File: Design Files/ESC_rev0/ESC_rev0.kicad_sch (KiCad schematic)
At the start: 0 parts

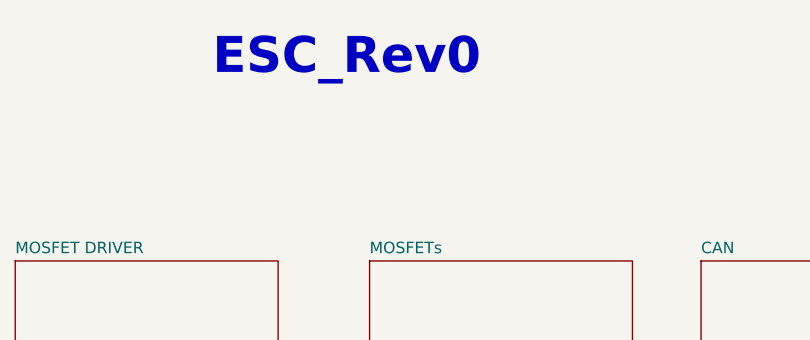
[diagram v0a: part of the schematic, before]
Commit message: update 6
gate driver completion and mosfet init
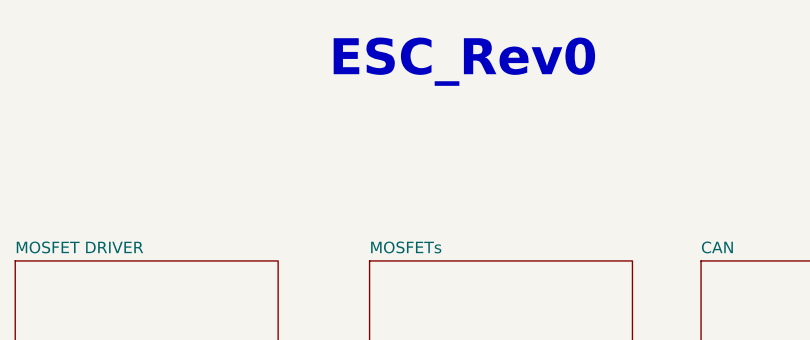
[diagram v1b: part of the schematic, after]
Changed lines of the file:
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@@
 	(text "${TITLE}"
 		(exclude_from_sim no)
-		(at 130.81 21.844 0)
+		(at 143.764 22.098 0)
 		(effects
 			(font

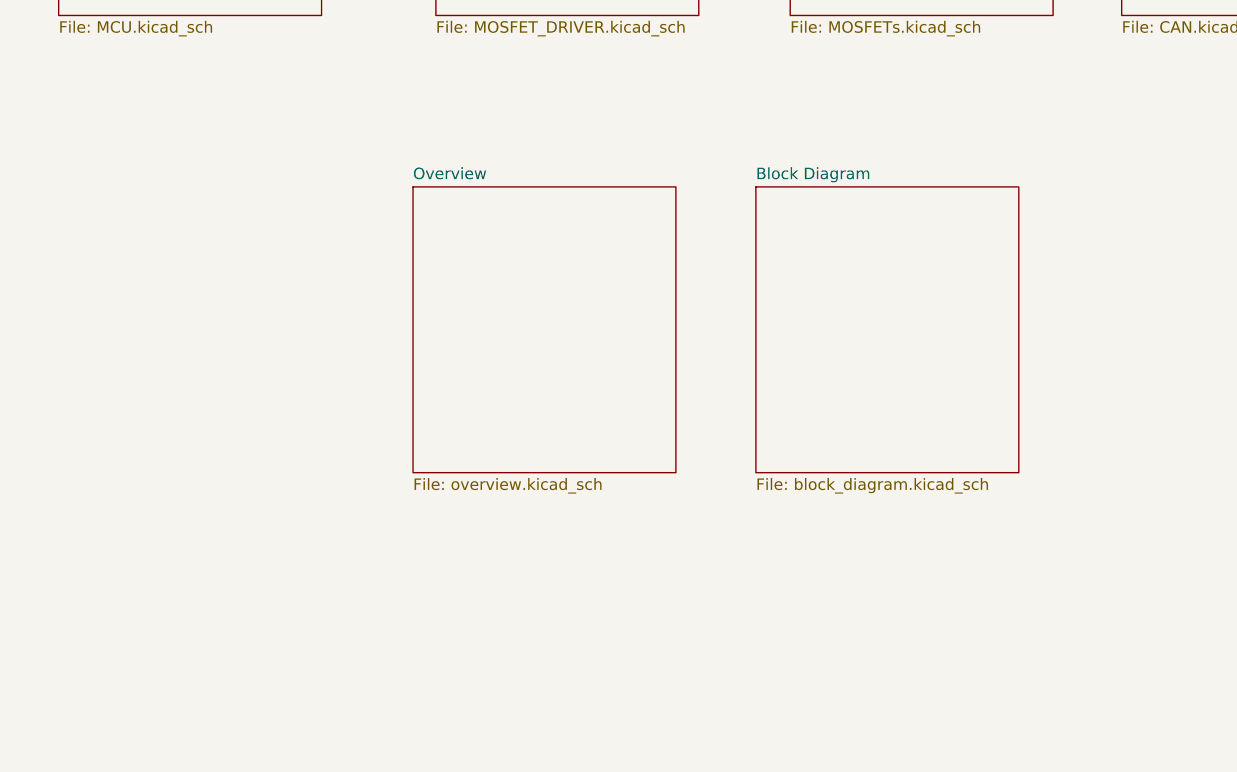
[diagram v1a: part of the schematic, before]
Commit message: update 8
conclusion of mosfets and input protection; can almost concluded
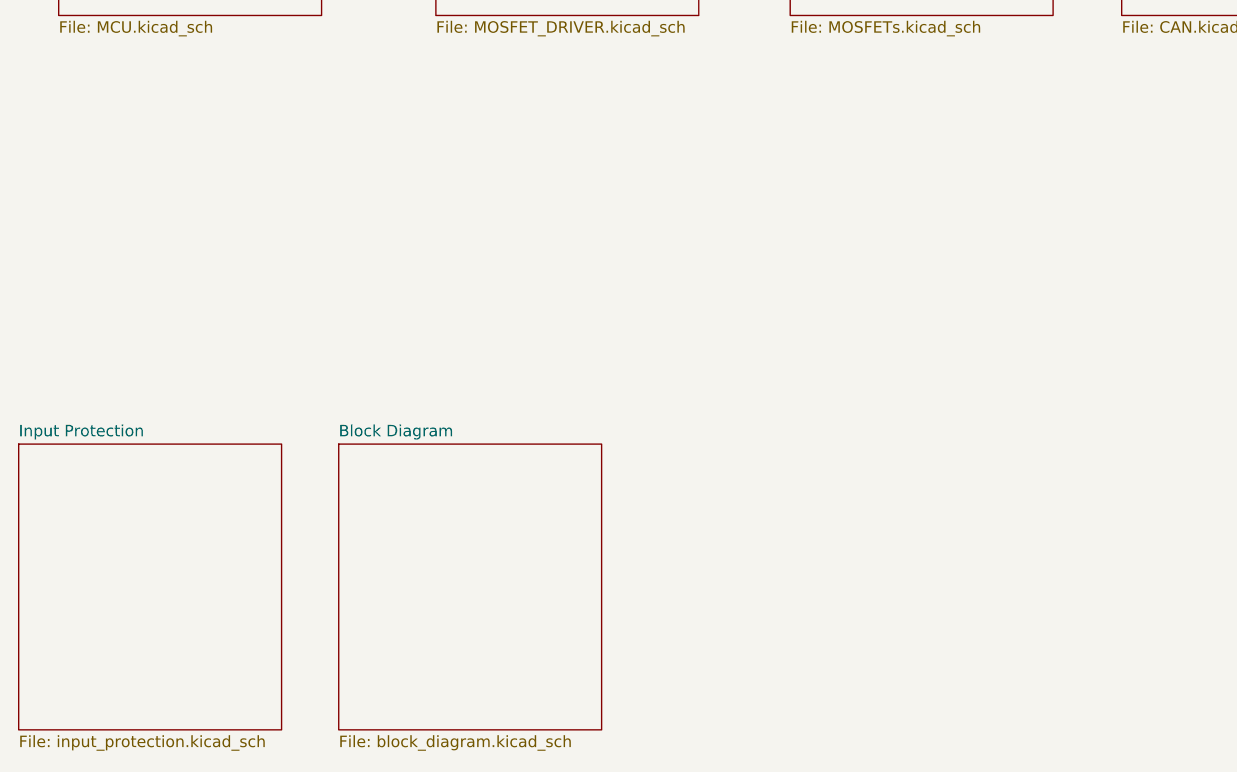
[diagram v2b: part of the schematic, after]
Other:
- sheet Overview renamed Input Protection
- sheet Input Protection: file overview.kicad_sch -> input_protection.kicad_sch
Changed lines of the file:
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@@
 	)
 	(sheet
-		(at 91.44 95.25)
+		(at 47.625 123.825)
 		(size 29.21 31.75)
 		(fields_autoplaced yes)
@@
 			(color 0 0 0 0.0000)
 		)
-		(property "Sheetname" "Overview"
-			(at 91.44 94.5384 0)
+		(property "Sheetname" "Input Protection"
+			(at 47.625 123.1134 0)
 			(effects
 				(font
@@
 			)
 		)
-		(property "Sheetfile" "overview.kicad_sch"
-			(at 91.44 127.5846 0)
+		(property "Sheetfile" "input_protection.kicad_sch"
+			(at 47.625 156.1596 0)
 			(effects
 				(font
@@
 	)
 	(sheet
-		(at 129.54 95.25)
+		(at 83.185 123.825)
 		(size 29.21 31.75)
 		(fields_autoplaced yes)
@@
 		)
 		(property "Sheetname" "Block Diagram"
-			(at 129.54 94.5384 0)
+			(at 83.185 123.1134 0)
 			(effects
 				(font
@@
 		)
 		(property "Sheetfile" "block_diagram.kicad_sch"
-			(at 129.54 127.5846 0)
+			(at 83.185 156.1596 0)
 			(effects
 				(font

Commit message: update 9
filters and USB complete
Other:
- added sheet USB (USB.kicad_sch)
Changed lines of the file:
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@@
+	)
+	(sheet
+		(at 121.92 124.46)
+		(size 29.21 31.75)
+		(fields_autoplaced yes)
+		(stroke
+			(width 0.1524)
+			(type solid)
+		)
+		(fill
+			(color 0 0 0 0.0000)
+		)
+		(property "Sheetname" "USB"
+			(at 121.92 123.7484 0)
+			(effects
+				(font
+					(size 1.27 1.27)
+				)
+				(justify left bottom)
+			)
+		)
+		(property "Sheetfile" "USB.kicad_sch"
+			(at 121.92 156.7946 0)
+			(effects
+				(font
+					(size 1.27 1.27)
+				)
+				(justify left top)
+			)
+		)
+		(instances
+			(project "ESC_rev0"
+				(path "/7906e740-34c4-4b06-b70f-1daa08872946"
+					(page "9")
+				)
+			)
+		)
 	)
 	(sheet

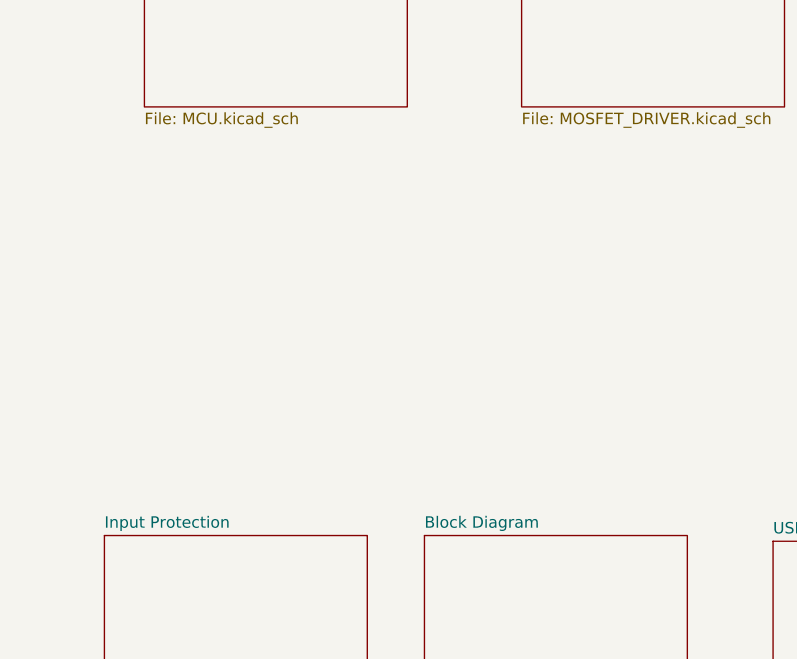
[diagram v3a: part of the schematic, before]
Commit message: update10
modifications to root page, completion of pages step_down and mechanical
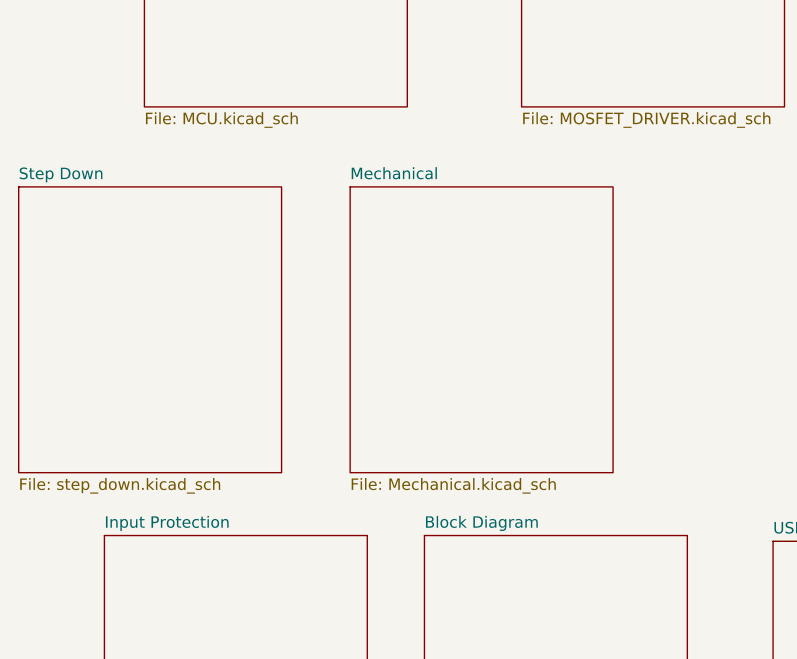
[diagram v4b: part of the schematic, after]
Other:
- added sheet Mechanical (Mechanical.kicad_sch)
- added sheet Step Down (step_down.kicad_sch)
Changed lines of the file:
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@@
+	)
+	(sheet
+		(at 38.1 85.09)
+		(size 29.21 31.75)
+		(fields_autoplaced yes)
+		(stroke
+			(width 0.1524)
+			(type solid)
+		)
+		(fill
+			(color 0 0 0 0.0000)
+		)
+		(property "Sheetname" "Step Down"
+			(at 38.1 84.3784 0)
+			(effects
+				(font
+					(size 1.27 1.27)
+				)
+				(justify left bottom)
+			)
+		)
+		(property "Sheetfile" "step_down.kicad_sch"
+			(at 38.1 117.4246 0)
+			(effects
+				(font
+					(size 1.27 1.27)
+				)
+				(justify left top)
+			)
+		)
+		(instances
+			(project "ESC_rev0"
+				(path "/7906e740-34c4-4b06-b70f-1daa08872946"
+					(page "10")
+				)
+			)
+		)
 	)
 	(sheet
@@
 				)
 			)
+		)
+	)
+	(sheet
+		(at 74.93 85.09)
+		(size 29.21 31.75)
+		(fields_autoplaced yes)
+		(stroke
+			(width 0.1524)
+			(type solid)
+		)
+		(fill
+			(color 0 0 0 0.0000)
+		)
+		(property "Sheetname" "Mechanical"
+			(at 74.93 84.3784 0)
+			(effects
+				(font
+					(size 1.27 1.27)
+				)
+				(justify left bottom)
+			)
+		)
+		(property "Sheetfile" "Mechanical.kicad_sch"
+			(at 74.93 117.4246 0)
+			(effects
+				(font
+					(size 1.27 1.27)
+				)
+				(justify left top)
+			)
+		)
+		(instances
+			(project "ESC_rev0"
+				(path "/7906e740-34c4-4b06-b70f-1daa08872946"
+					(page "11")
+				)
+			)

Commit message: update11
root page base complete
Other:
- note added: "1"
- note added: "10"
- note added: "2"
- note added: "3"
- note added: "4"
- note added: "5"
- note added: "6"
- note added: "7"
- note added: "8"
- note added: "9"
- note added: "Block Diagram"
- note added: "Board Image Back"
- note added: "Board Image Front"
- note added: "CAN"
- note added: "DRAFT"
- note added: "Date: 2025/01/07"
- note added: "Filters"
- note added: "Index"
- note added: "Input Protection"
- note added: "MCU"
- note added: "MOSFET Driver"
- note added: "MOSFETs"
- note added: "Mechanical"
- note added: "Page #"
- note added: "Project Status:"
- note added: "Revision: ${REVISION}"
- note added: "Step Down"
- note added: "USB"
- note added: "Variant: No variants"

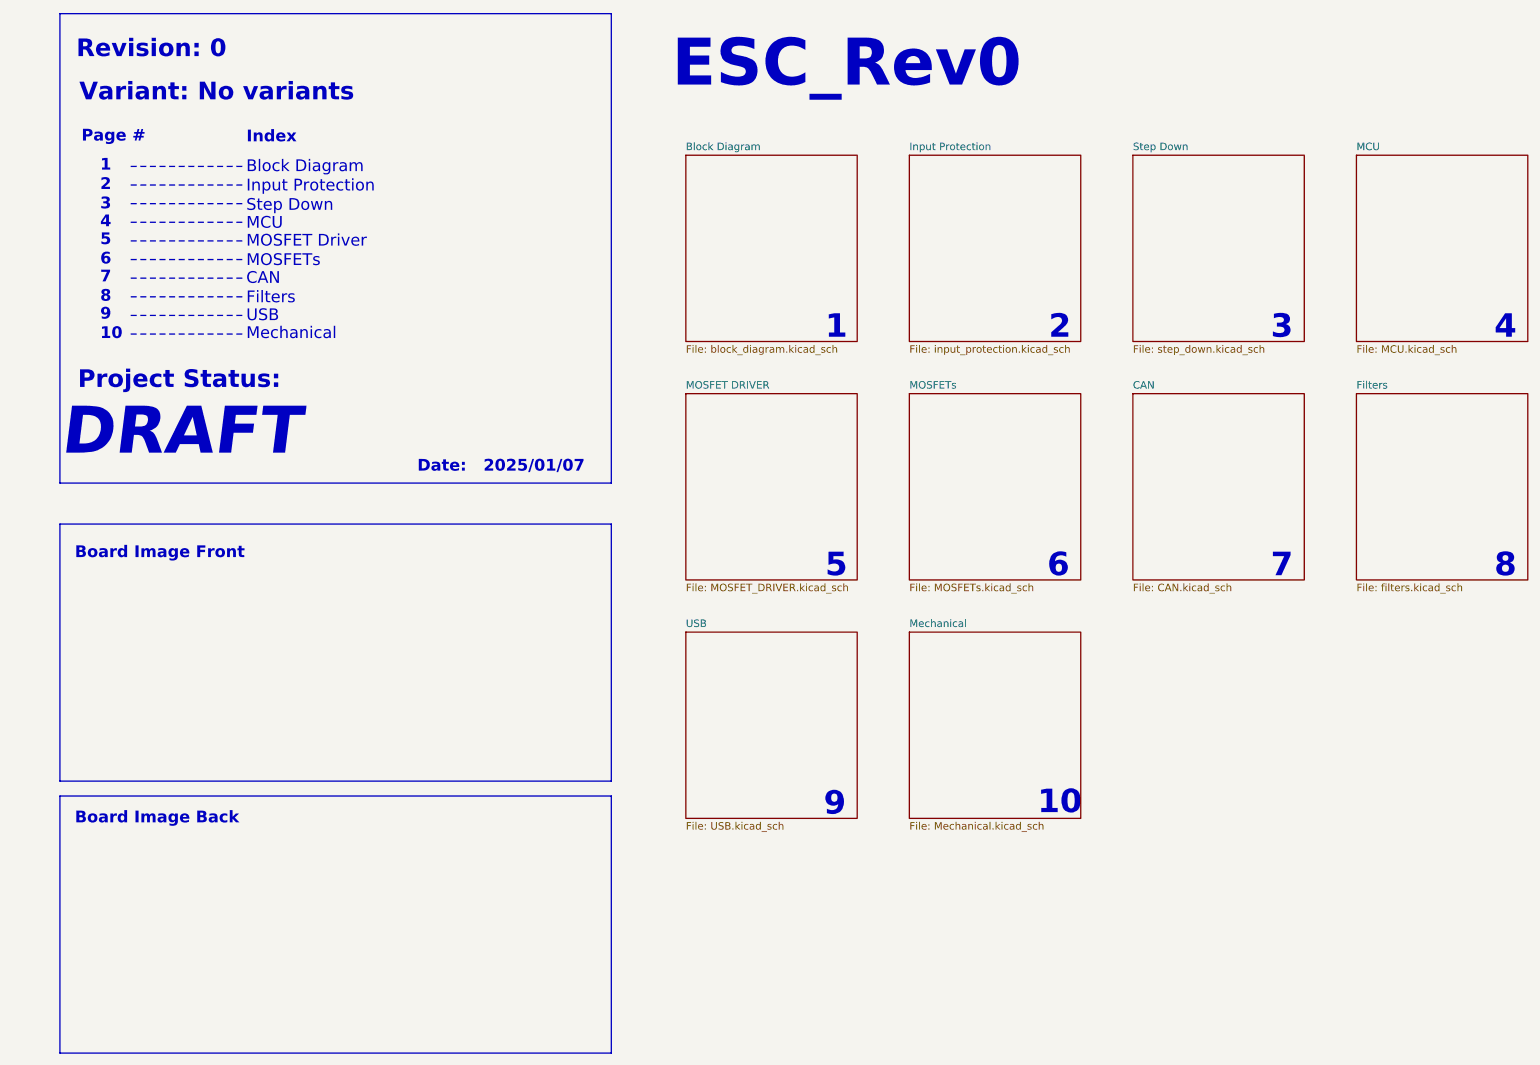
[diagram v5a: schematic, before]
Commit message: update 21
DRC checked, all problems solved. Created Custom Rules to following JLCPCB most important capabilities. Relevant modifications on tracks, components positions and to copper pours were made. Board images were updated in the schematics.
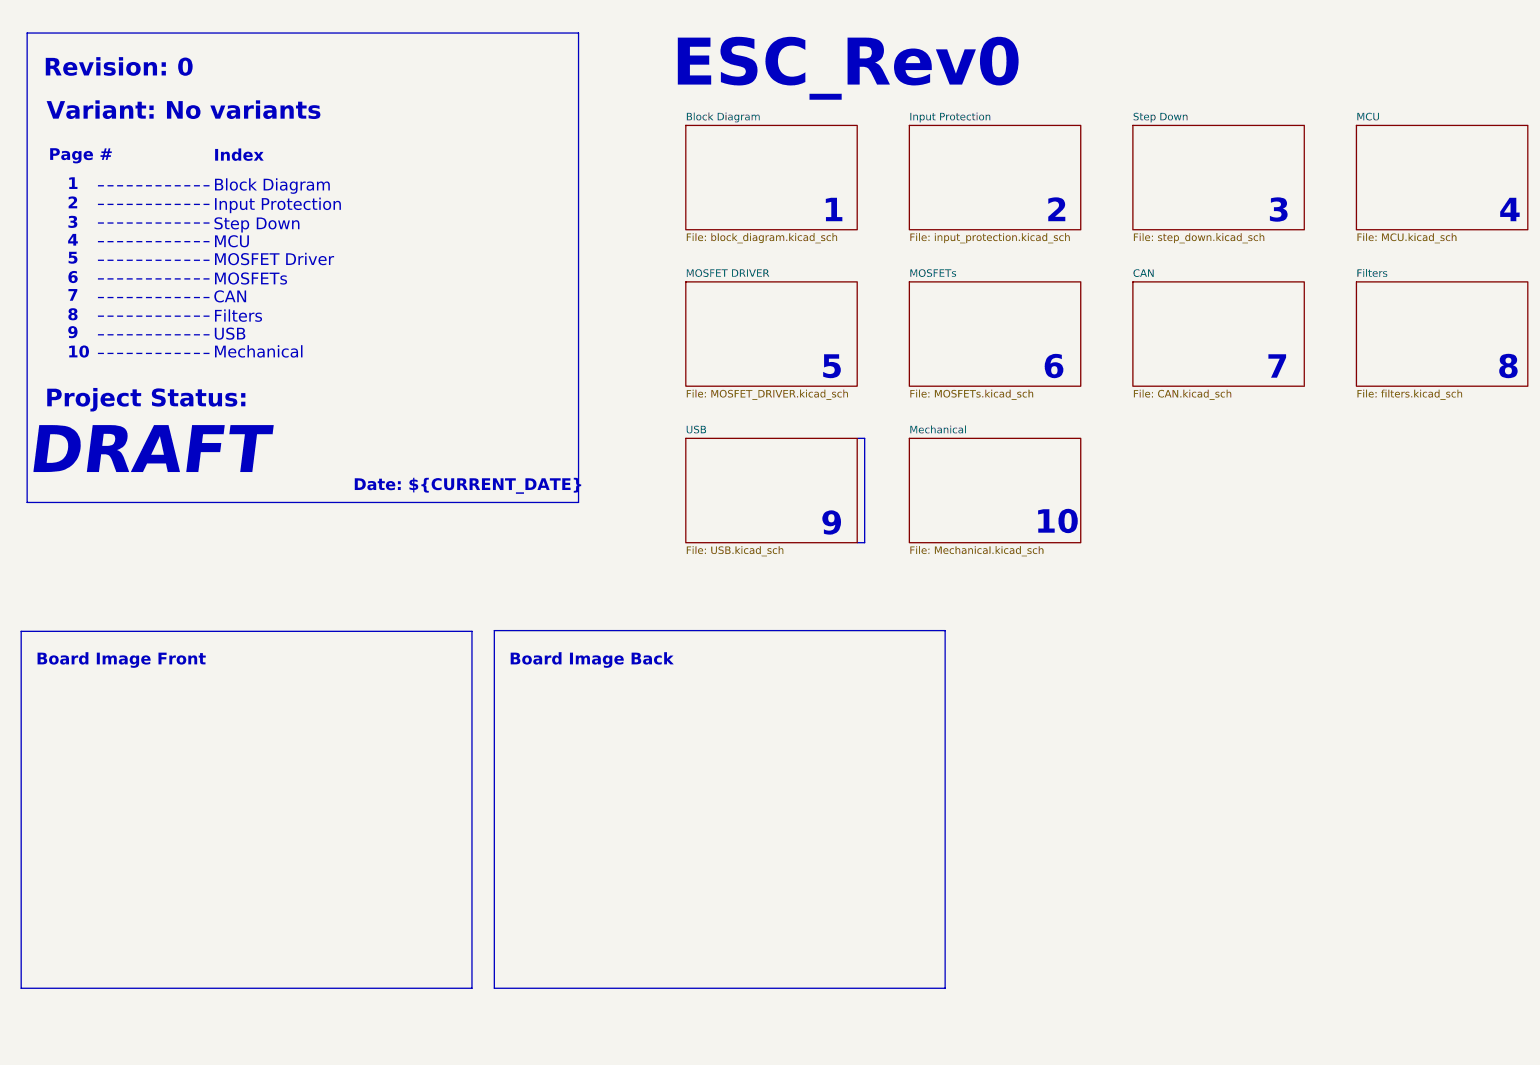
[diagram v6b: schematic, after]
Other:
- note added: "Date: ${CURRENT_DATE}"
- note removed: "Date: 2025/01/07"
